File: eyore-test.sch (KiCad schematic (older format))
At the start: 29 parts, among them P1 USB_5PIN_SHELL, P2 CONN_01X04, P3 CONN_01X02, SW1 SW_PUSHBUTTON, SW2 SW_PUSHBUTTON, U1 LD1117S33CTR, U2 STM32F072C8, U3 ESP-12E, U4 ESP-12E

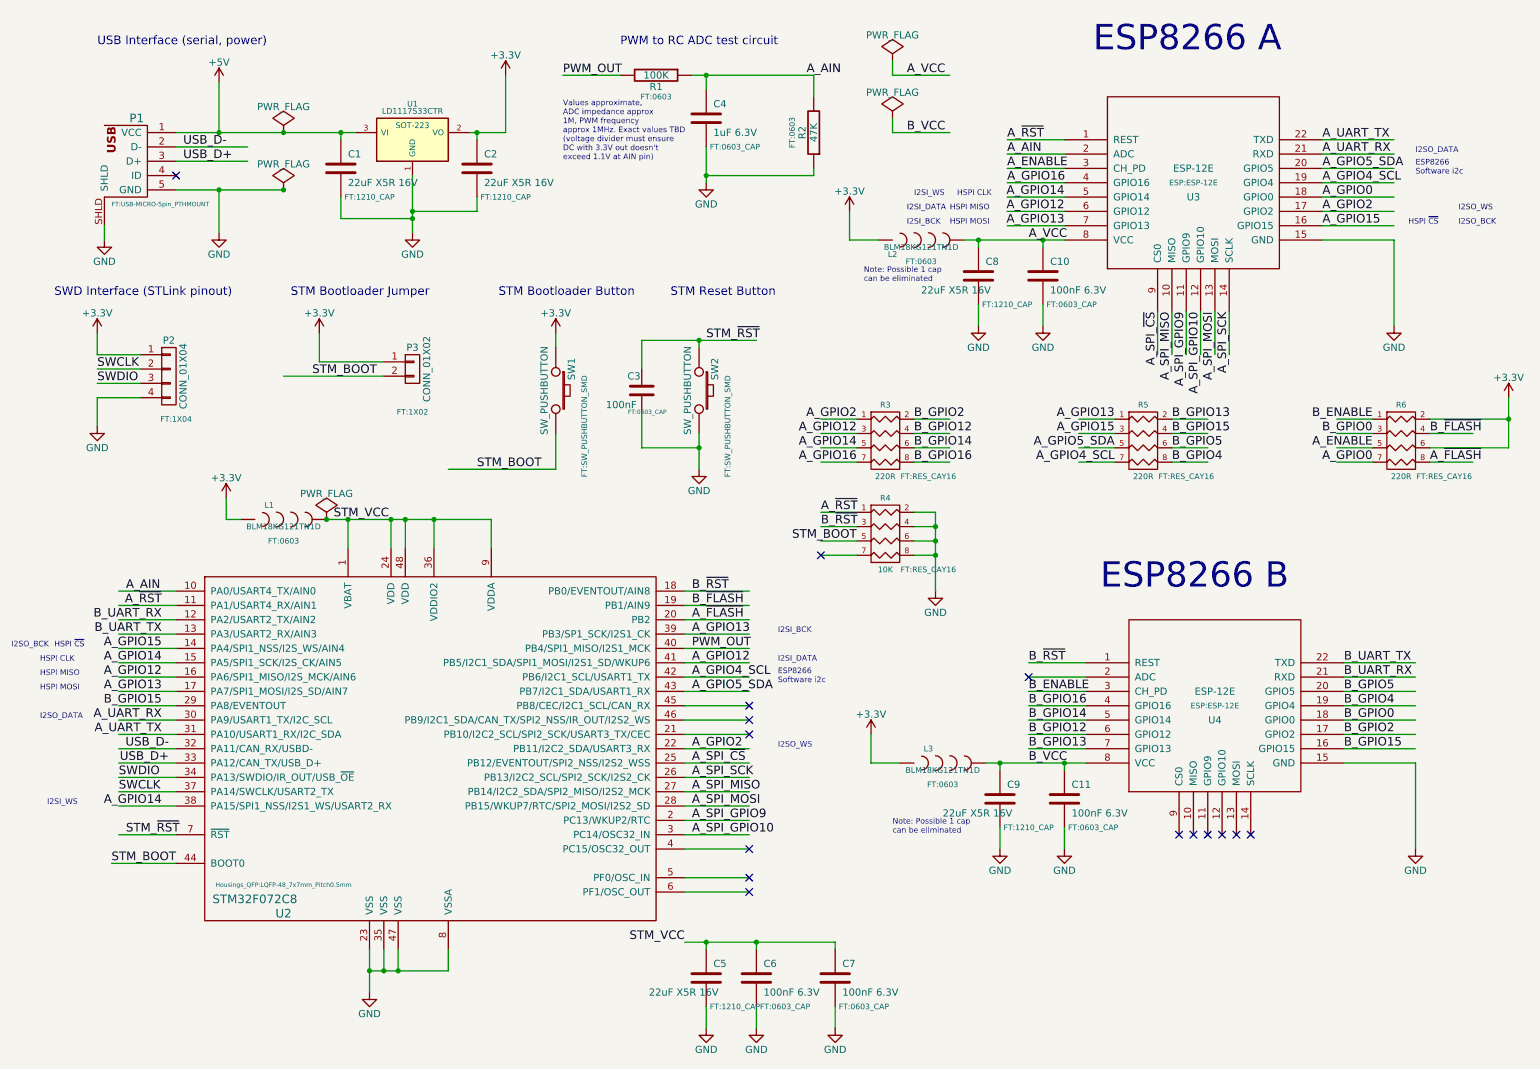
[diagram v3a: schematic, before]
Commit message: Part routed, but I think approach was wrong
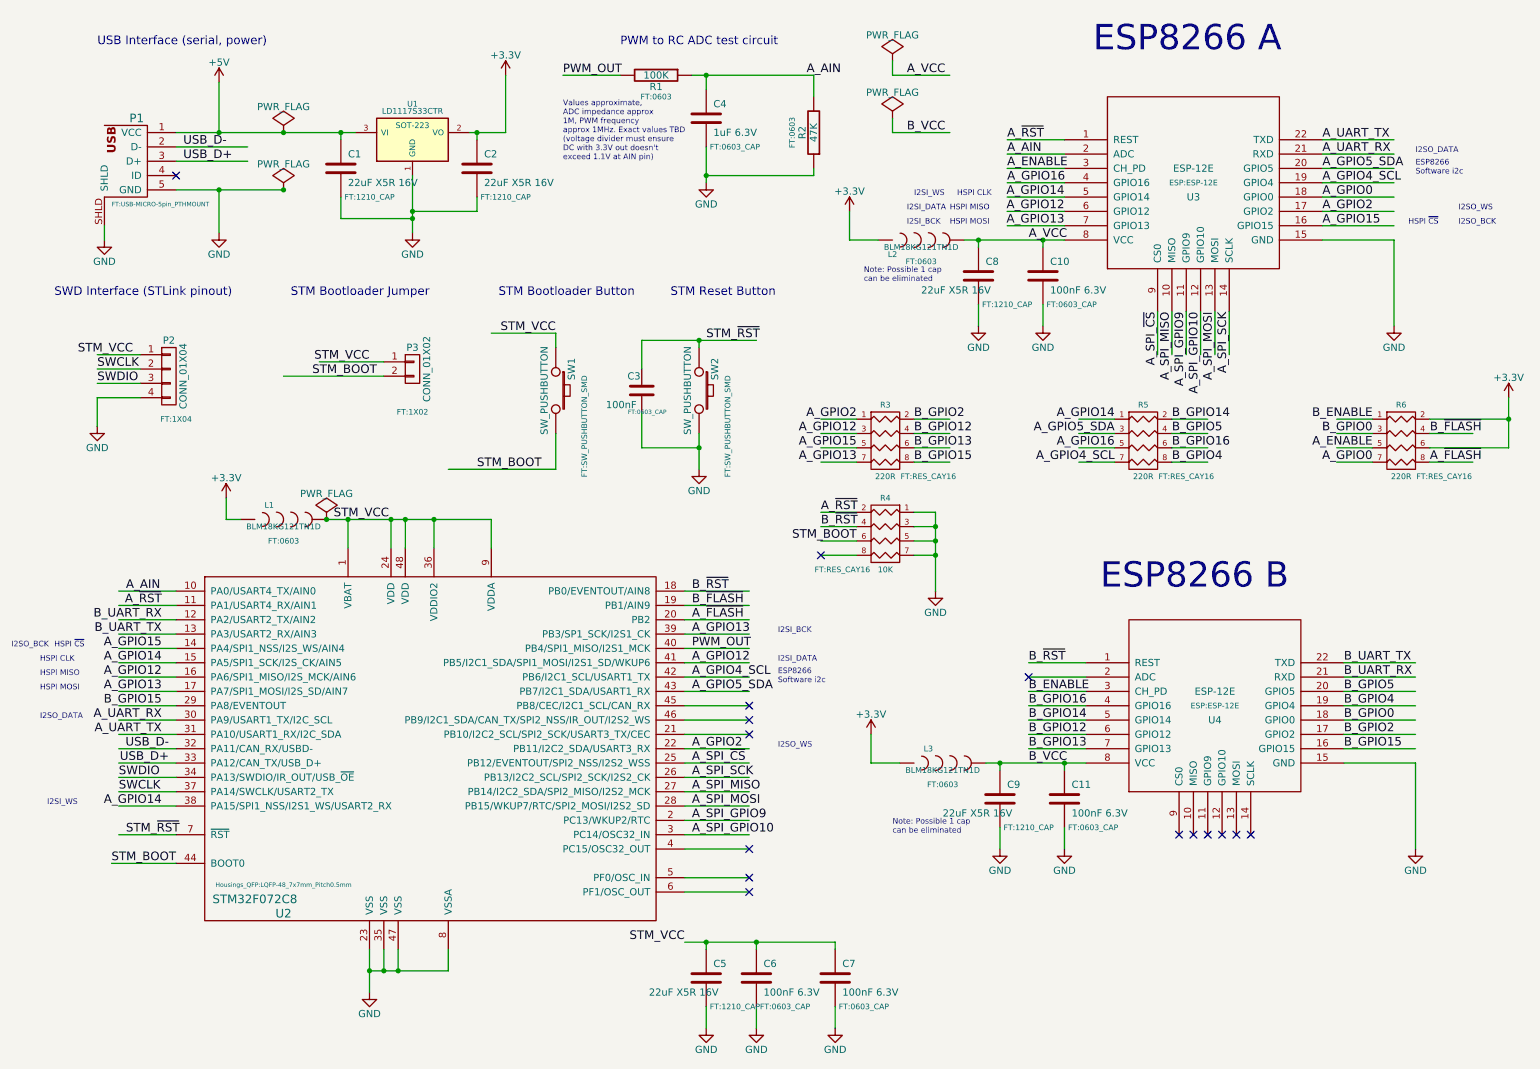
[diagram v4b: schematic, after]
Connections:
- wire segments 190 -> 189
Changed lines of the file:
@@
 $EndComp
 $Comp
-L +3.3V #PWR05
-U 1 1 56306B97
-P 1100 2700
-F 0 "#PWR05" H 1100 2550 50  0001 C CNN
-F 1 "+3.3V" H 1100 2840 50  0000 C CNN
-F 2 "" H 1100 2700 60  0000 C CNN
-F 3 "" H 1100 2700 60  0000 C CNN
-	1    1100 2700
-	1    0    0    -1
-$EndComp
-$Comp
-L GND #PWR06
+L GND #PWR05
 U 1 1 56306BF9
 P 1100 3350
-F 0 "#PWR06" H 1100 3100 50  0001 C CNN
+F 0 "#PWR05" H 1100 3100 50  0001 C CNN
 F 1 "GND" H 1100 3200 50  0000 C CNN
 F 2 "" H 1100 3350 60  0000 C CNN
@@
 $EndComp
 $Comp
-L GND #PWR07
+L GND #PWR06
 U 1 1 56316BE1
 P 3300 2000
-F 0 "#PWR07" H 3300 1750 50  0001 C CNN
+F 0 "#PWR06" H 3300 1750 50  0001 C CNN
 F 1 "GND" H 3300 1850 50  0000 C CNN
 F 2 "" H 3300 2000 60  0000 C CNN
@@
 A_GPIO5_SDA
 $Comp
-L GND #PWR08
+L GND #PWR07
 U 1 1 5631751A
 P 10150 2650
-F 0 "#PWR08" H 10150 2400 50  0001 C CNN
+F 0 "#PWR07" H 10150 2400 50  0001 C CNN
 F 1 "GND" H 10150 2500 50  0000 C CNN
 F 2 "" H 10150 2650 60  0000 C CNN
@@
 $EndComp
 $Comp
-L +3.3V #PWR09
+L +3.3V #PWR08
 U 1 1 5631769D
 P 6350 1850
-F 0 "#PWR09" H 6350 1700 50  0001 C CNN
+F 0 "#PWR08" H 6350 1700 50  0001 C CNN
 F 1 "+3.3V" H 6350 1990 50  0000 C CNN
 F 2 "" H 6350 1850 60  0000 C CNN
@@
 A_GPIO12
 $Comp
-L GND #PWR010
+L GND #PWR09
 U 1 1 56317DB5
 P 7700 2650
-F 0 "#PWR010" H 7700 2400 50  0001 C CNN
+F 0 "#PWR09" H 7700 2400 50  0001 C CNN
 F 1 "GND" H 7700 2500 50  0000 C CNN
 F 2 "" H 7700 2650 60  0000 C CNN
@@
 $EndComp
 $Comp
-L GND #PWR011
+L GND #PWR010
 U 1 1 56318159
 P 7250 2650
-F 0 "#PWR011" H 7250 2400 50  0001 C CNN
+F 0 "#PWR010" H 7250 2400 50  0001 C CNN
 F 1 "GND" H 7250 2500 50  0000 C CNN
 F 2 "" H 7250 2650 60  0000 C CNN
@@
 B_GPIO5
 $Comp
-L GND #PWR012
+L GND #PWR011
 U 1 1 56319095
 P 10300 6300
-F 0 "#PWR012" H 10300 6050 50  0001 C CNN
+F 0 "#PWR011" H 10300 6050 50  0001 C CNN
 F 1 "GND" H 10300 6150 50  0000 C CNN
 F 2 "" H 10300 6300 60  0000 C CNN
@@
 $EndComp
 $Comp
-L +3.3V #PWR013
+L +3.3V #PWR012
 U 1 1 5631909C
 P 6500 5500
-F 0 "#PWR013" H 6500 5350 50  0001 C CNN
+F 0 "#PWR012" H 6500 5350 50  0001 C CNN
 F 1 "+3.3V" H 6500 5640 50  0000 C CNN
 F 2 "" H 6500 5500 60  0000 C CNN
@@
 B_GPIO12
 $Comp
-L GND #PWR014
+L GND #PWR013
 U 1 1 563190B5
 P 7850 6300
-F 0 "#PWR014" H 7850 6050 50  0001 C CNN
+F 0 "#PWR013" H 7850 6050 50  0001 C CNN
 F 1 "GND" H 7850 6150 50  0000 C CNN
 F 2 "" H 7850 6300 60  0000 C CNN
@@
 $EndComp
 $Comp
-L GND #PWR015
+L GND #PWR014
 U 1 1 563190C4
 P 7400 6300
-F 0 "#PWR015" H 7400 6050 50  0001 C CNN
+F 0 "#PWR014" H 7400 6050 50  0001 C CNN
 F 1 "GND" H 7400 6150 50  0000 C CNN
 F 2 "" H 7400 6300 60  0000 C CNN
@@
 A_AIN
 NoConn ~ 7600 5100
-Text Label 6400 3600 2    60   ~ 0
+Text Label 8200 3500 2    60   ~ 0
 A_GPIO16
-Text Label 6400 3500 2    60   ~ 0
+Text Label 8200 3300 2    60   ~ 0
 A_GPIO14
 Text Label 10000 3600 2    60   ~ 0
@@
 Text Label 6800 3400 0    60   ~ 0
 B_GPIO12
+Text Label 8600 3300 0    60   ~ 0
+B_GPIO14
+Text Label 8600 3500 0    60   ~ 0
+B_GPIO16
 Text Label 6800 3500 0    60   ~ 0
-B_GPIO14
+B_GPIO13
 Text Label 6800 3600 0    60   ~ 0
-B_GPIO16
-Text Label 8600 3300 0    60   ~ 0
-B_GPIO13
-Text Label 8600 3400 0    60   ~ 0
 B_GPIO15
 Text Label 8600 3600 0    60   ~ 0
 B_GPIO4
-Text Label 8600 3500 0    60   ~ 0
+Text Label 8600 3400 0    60   ~ 0
 B_GPIO5
 Text Label 8200 3600 2    60   ~ 0
 A_GPIO4_SCL
-Text Label 8200 3500 2    60   ~ 0
+Text Label 8200 3400 2    60   ~ 0
 A_GPIO5_SDA
 Text Label 5250 5200 0    60   ~ 0
@@
 Text Label 1650 6400 2    60   ~ 0
 STM_BOOT
-$Comp
-L +3.3V #PWR016
-U 1 1 5631C4F8
-P 2650 2700
-F 0 "#PWR016" H 2650 2550 50  0001 C CNN
-F 1 "+3.3V" H 2650 2840 50  0000 C CNN
-F 2 "" H 2650 2700 60  0000 C CNN
-F 3 "" H 2650 2700 60  0000 C CNN
-	1    2650 2700
-	1    0    0    -1
-$EndComp
 Text Notes 2450 2450 0    60   ~ 0
 STM Bootloader Jumper\n
@@
 PWM to RC ADC test circuit
 $Comp
-L GND #PWR017
+L GND #PWR015
 U 1 1 5631DA5C
 P 5350 1650
-F 0 "#PWR017" H 5350 1400 50  0001 C CNN
+F 0 "#PWR015" H 5350 1400 50  0001 C CNN
 F 1 "GND" H 5350 1500 50  0000 C CNN
 F 2 "" H 5350 1650 60  0000 C CNN
@@
 	-1   0    0    1
 $EndComp
-Text Label 8200 3300 2    60   ~ 0
+Text Label 6400 3600 2    60   ~ 0
 A_GPIO13
 Text Label 6400 3400 2    60   ~ 0
@@
 A_AIN
 $Comp
-L +3.3V #PWR018
+L +3.3V #PWR016
 U 1 1 563276CF
 P 2000 3850
-F 0 "#PWR018" H 2000 3700 50  0001 C CNN
+F 0 "#PWR016" H 2000 3700 50  0001 C CNN
 F 1 "+3.3V" H 2000 3990 50  0000 C CNN
 F 2 "" H 2000 3850 60  0000 C CNN
@@
 $EndComp
 $Comp
-L GND #PWR019
+L GND #PWR017
 U 1 1 563280A5
 P 5700 7550
-F 0 "#PWR019" H 5700 7300 50  0001 C CNN
+F 0 "#PWR017" H 5700 7300 50  0001 C CNN
 F 1 "GND" H 5700 7400 50  0000 C CNN
 F 2 "" H 5700 7550 60  0000 C CNN
@@
 $EndComp
 $Comp
-L GND #PWR020
+L GND #PWR018
 U 1 1 563280B2
 P 5350 7550
-F 0 "#PWR020" H 5350 7300 50  0001 C CNN
+F 0 "#PWR018" H 5350 7300 50  0001 C CNN
 F 1 "GND" H 5350 7400 50  0000 C CNN
 F 2 "" H 5350 7550 60  0000 C CNN
@@
 STM_VCC
 $Comp
-L GND #PWR021
+L GND #PWR019
 U 1 1 563282F2
 P 3000 7300
-F 0 "#PWR021" H 3000 7050 50  0001 C CNN
+F 0 "#PWR019" H 3000 7050 50  0001 C CNN
 F 1 "GND" H 3000 7150 50  0000 C CNN
 F 2 "" H 3000 7300 60  0000 C CNN
@@
 	0    1    1    0
 $EndComp
-$Comp
-L +3.3V #PWR022
-U 1 1 563293FD
-P 4300 2700
-F 0 "#PWR022" H 4300 2550 50  0001 C CNN
-F 1 "+3.3V" H 4300 2840 50  0000 C CNN
-F 2 "" H 4300 2700 60  0000 C CNN
-F 3 "" H 4300 2700 60  0000 C CNN
-	1    4300 2700
-	1    0    0    -1
-$EndComp
 Text Label 5350 2750 0    60   ~ 0
 STM_~RST
 $Comp
-L GND #PWR023
+L GND #PWR020
 U 1 1 56329666
 P 5300 3650
-F 0 "#PWR023" H 5300 3400 50  0001 C CNN
+F 0 "#PWR020" H 5300 3400 50  0001 C CNN
 F 1 "GND" H 5300 3500 50  0000 C CNN
 F 2 "" H 5300 3650 60  0000 C CNN
@@
 Text Notes 5100 2450 0    60   ~ 0
 STM Reset Button
-Text Label 8200 3400 2    60   ~ 0
+Text Label 6400 3500 2    60   ~ 0
 A_GPIO15
 $Comp
-L +3.3V #PWR024
+L +3.3V #PWR021
 U 1 1 5632C27E
 P 10950 3150
-F 0 "#PWR024" H 10950 3000 50  0001 C CNN
+F 0 "#PWR021" H 10950 3000 50  0001 C CNN
 F 1 "+3.3V" H 10950 3290 50  0000 C CNN
 F 2 "" H 10950 3150 60  0000 C CNN
@@
 $EndComp
 $Comp
-L PWR_FLAG #FLG025
+L PWR_FLAG #FLG022
 U 1 1 5632C368
 P 6650 800
-F 0 "#FLG025" H 6650 895 50  0001 C CNN
+F 0 "#FLG022" H 6650 895 50  0001 C CNN
 F 1 "PWR_FLAG" H 6650 980 50  0000 C CNN
 F 2 "" H 6650 800 60  0000 C CNN
@@
 A_VCC
 $Comp
-L PWR_FLAG #FLG026
+L PWR_FLAG #FLG023
 U 1 1 5632C4E6
 P 6650 1200
-F 0 "#FLG026" H 6650 1295 50  0001 C CNN
+F 0 "#FLG023" H 6650 1295 50  0001 C CNN
 F 1 "PWR_FLAG" H 6650 1380 50  0000 C CNN
 F 2 "" H 6650 1200 60  0000 C CNN
@@
 B_VCC
 $Comp
-L PWR_FLAG #FLG027
+L PWR_FLAG #FLG024
 U 1 1 5632C7E0
 P 2700 4000
-F 0 "#FLG027" H 2700 4095 50  0001 C CNN
+F 0 "#FLG024" H 2700 4095 50  0001 C CNN
 F 1 "PWR_FLAG" H 2700 4180 50  0000 C CNN
 F 2 "" H 2700 4000 60  0000 C CNN
@@
 $EndComp
 $Comp
-L PWR_FLAG #FLG028
+L PWR_FLAG #FLG025
 U 1 1 5632CBA7
 P 2400 1700
-F 0 "#FLG028" H 2400 1795 50  0001 C CNN
+F 0 "#FLG025" H 2400 1795 50  0001 C CNN
 F 1 "PWR_FLAG" H 2400 1880 50  0000 C CNN
 F 2 "" H 2400 1700 60  0000 C CNN
@@
 A_GPIO2
 $Comp
-L PWR_FLAG #FLG029
+L PWR_FLAG #FLG026
 U 1 1 5632D5E0
 P 2400 1300
-F 0 "#FLG029" H 2400 1395 50  0001 C CNN
+F 0 "#FLG026" H 2400 1395 50  0001 C CNN
 F 1 "PWR_FLAG" H 2400 1480 50  0000 C CNN
 F 2 "" H 2400 1300 60  0000 C CNN
@@
 Connection ~ 3150 4000
 Wire Wire Line
-	3150 4200 3150 4000
+	3150 4000 3150 4200
 Wire Wire Line
 	3250 4000 3250 4200
@@
 	5250 900  6100 900
 Wire Wire Line
-	2650 2900 2650 2700
-Wire Wire Line
 	3100 3000 2400 3000
 Wire Wire Line
@@
 	6400 3300 6150 3300
 Wire Wire Line
-	7850 5750 7850 5700
+	7850 5700 7850 5750
 Wire Wire Line
 	7400 6150 7400 6300
@@
 	8000 5000 7600 5000
 Wire Wire Line
-	7700 2100 7700 2050
+	7700 2050 7700 2100
 Wire Wire Line
 	7250 2500 7250 2650
@@
 Connection ~ 3300 1900
 Wire Wire Line
-	2800 1900 3300 1900
-Wire Wire Line
-	2800 1750 2800 1900
+	3300 1900 2800 1900
+Wire Wire Line
+	2800 1900 2800 1750
 Wire Wire Line
 	3300 1600 3300 2000
@@
 Connection ~ 2800 1300
 Wire Wire Line
-	2800 1350 2800 1300
+	2800 1300 2800 1350
 Wire Wire Line
 	1100 3150 1100 3350
@@
 Wire Wire Line
 	1400 2950 1100 2950
-Wire Wire Line
-	1100 2850 1100 2700
 Wire Wire Line
 	1400 2850 1100 2850
@@
 Connection ~ 5700 6950
 $Comp
-L GND #PWR030
+L GND #PWR027
 U 1 1 56425794
 P 6250 7550
-F 0 "#PWR030" H 6250 7300 50  0001 C CNN
+F 0 "#PWR027" H 6250 7300 50  0001 C CNN
 F 1 "GND" H 6250 7400 50  0000 C CNN
 F 2 "" H 6250 7550 60  0000 C CNN
@@
 F 3 "" H 6600 4300 60  0000 C CNN
 	1    6600 4300
-	1    0    0    -1
+	-1   0    0    -1
 $EndComp
 Wire Wire Line
@@
 	6950 3950 6950 4500
 $Comp
-L GND #PWR031
+L GND #PWR028
 U 1 1 56438AB2
 P 6950 4500
-F 0 "#PWR031" H 6950 4250 50  0001 C CNN
+F 0 "#PWR028" H 6950 4250 50  0001 C CNN
 F 1 "GND" H 6950 4350 50  0000 C CNN
 F 2 "" H 6950 4500 60  0000 C CNN
@@
 A_~FLASH
 Wire Wire Line
-	10950 3500 10950 3150
+	10950 3150 10950 3500
 Connection ~ 10950 3300
 Text Label 10400 3400 0    60   ~ 0
@@
 	10000 3600 9750 3600
 Wire Wire Line
-	10400 3500 10950 3500
+	10950 3500 10400 3500
 Text Label 10000 3400 2    60   ~ 0
 B_GPIO0
@@
 Wire Wire Line
 	10400 3400 10700 3400
+Text Label 1350 2850 2    60   ~ 0
+STM_VCC
+Text Label 3000 2900 2    60   ~ 0
+STM_VCC
+Wire Wire Line
+	4300 2700 3850 2700
+Text Label 4300 2700 2    60   ~ 0
+STM_VCC
 $EndSCHEMATC
